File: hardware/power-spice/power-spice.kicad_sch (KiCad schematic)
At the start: 15 parts, among them Q1 NMOS, Q2 NMOS

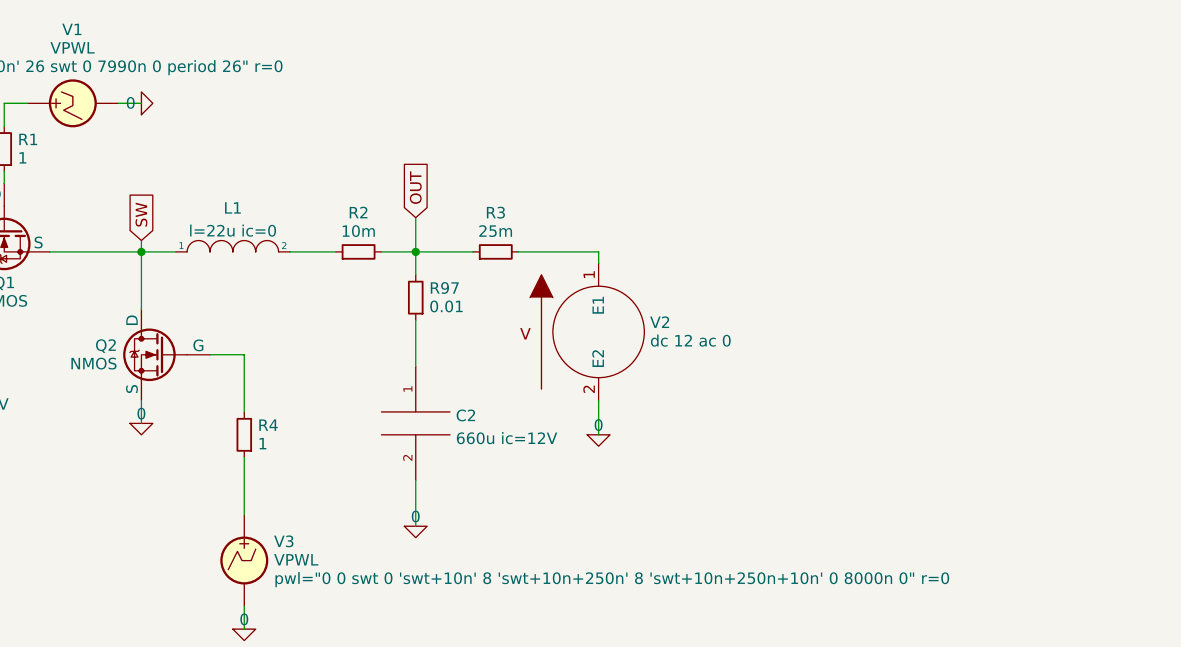
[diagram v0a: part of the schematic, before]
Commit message: Add PWM_V RC network to the simulation model.
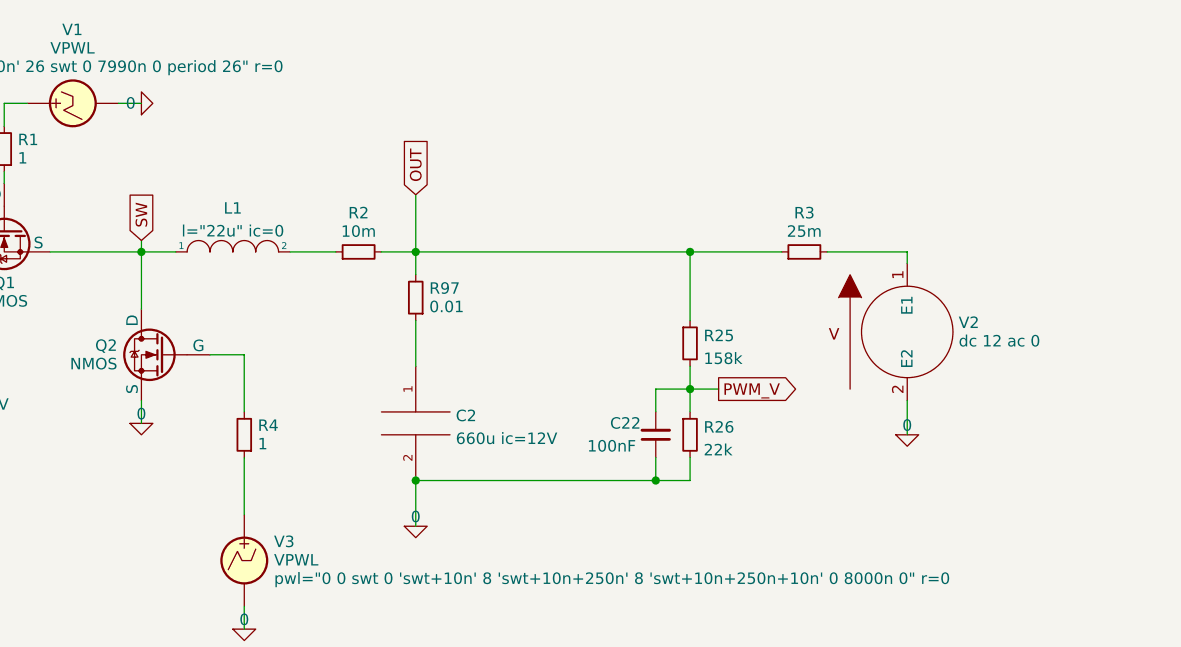
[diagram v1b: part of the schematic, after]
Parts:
- added C22: 100nF, Capacitor_SMD:C_0603_1608Metric_Pad1.08x0.95mm_HandSolder, symbol Device:C_Small
- added R25: 158k, Resistor_SMD:R_0805_2012Metric_Pad1.20x1.40mm_HandSolder, symbol Device:R_Small
- added R26: 22k, Resistor_SMD:R_0805_2012Metric_Pad1.20x1.40mm_HandSolder, symbol Device:R_Small
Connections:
- net 0: now also C22.1, R26.2
- net OUT: now also R25.1
- new net PWM_V: C22.2, R25.2, R26.1
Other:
- moved on the sheet: R3, V2

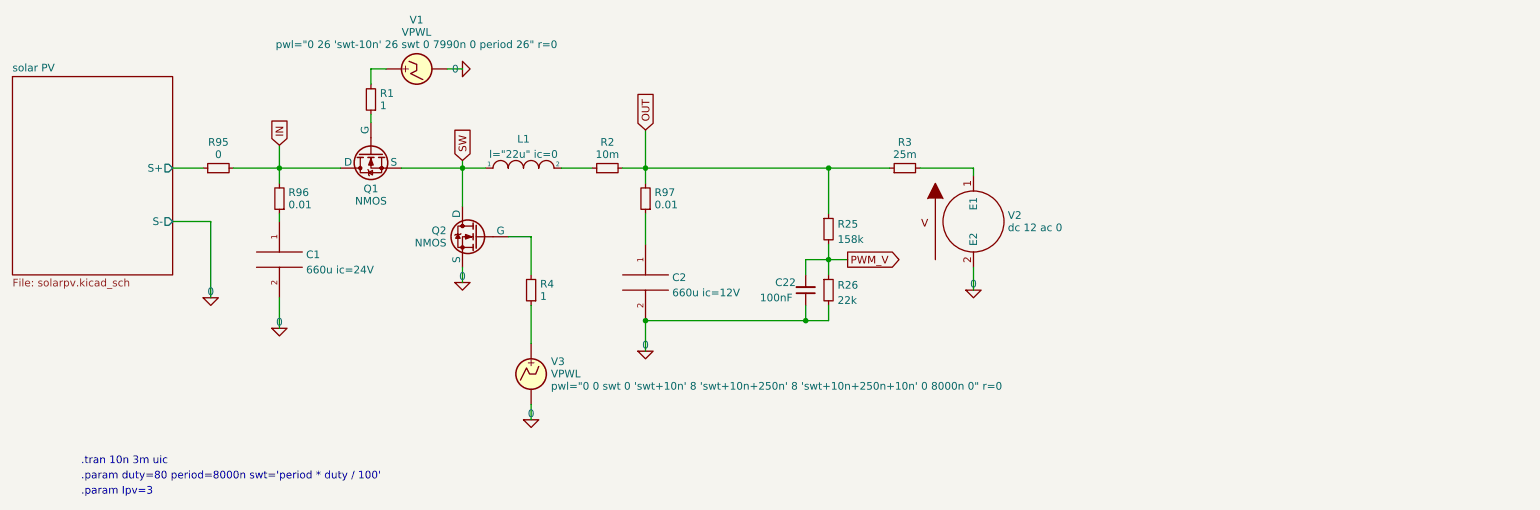
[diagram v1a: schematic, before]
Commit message: Add ouput stage to power-spice simulator.
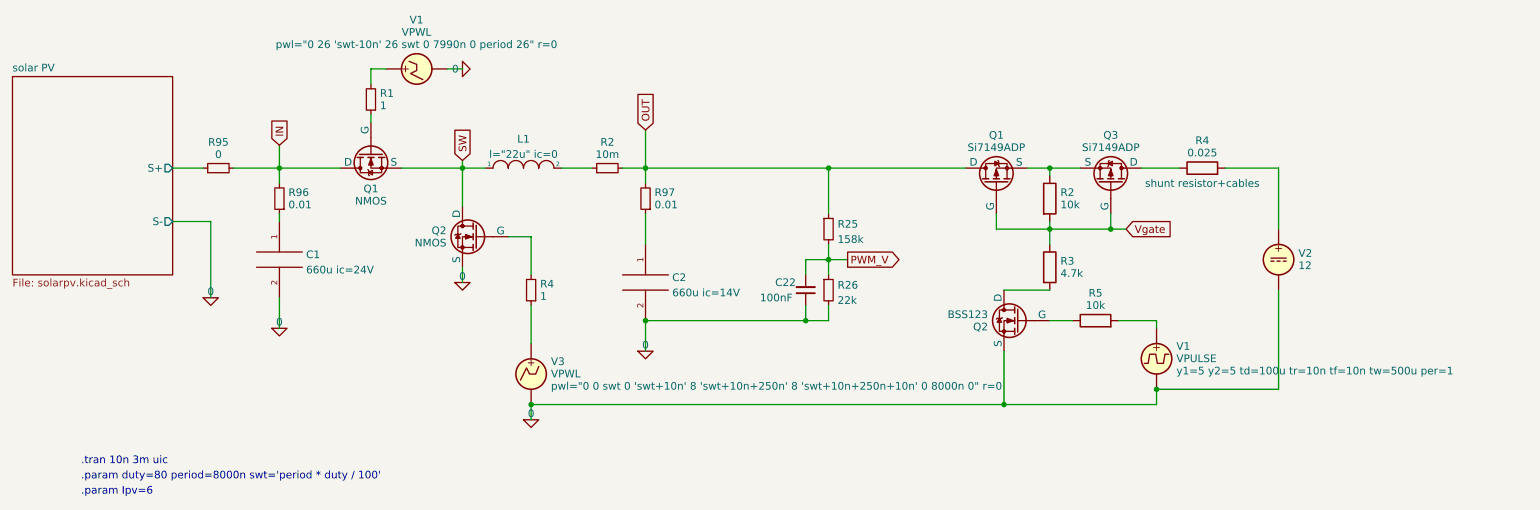
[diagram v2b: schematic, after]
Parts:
- removed R3: 25m, symbol Device:R_Small
- removed V2: dc 12 ac 0, symbol pspice:VSOURCE
- added Q1, Q3: Si7149ADP, symbol Simulation_SPICE:PMOS
- added Q2: BSS123, symbol Simulation_SPICE:NMOS
- added R2, R5: 10k, symbol Device:R
- added R3: 4.7k, symbol Device:R
- added R4: 0.025, symbol Device:R
- added V1: VPULSE, symbol Simulation_SPICE:VPULSE
- added V2: 12, symbol Simulation_SPICE:VDC
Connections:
- net 0: now also Q2.3 (S), V1.2, V2.2
- net OUT: now also Q1.1 (D)
- new net: Q2.2 (G), R5.1
- new net: R5.2, V1.1
- new net: Q2.1 (D), R3.2
- new net: Q3.1 (D), R4.1
- new net: R4.2, V2.1
- new net: Q1.3 (S), Q3.3 (S), R2.1
- new net Vgate: Q1.2 (G), Q3.2 (G), R2.2, R3.1
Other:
- note added: ".param Ipv=6"
- note removed: ".param Ipv=3"
